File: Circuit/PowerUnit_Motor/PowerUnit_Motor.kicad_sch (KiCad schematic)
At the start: 16 parts, among them J1 Conn_01x02_Pin, J10 Conn_01x02_Pin, J11 Conn_01x02_Pin, J2 Conn_01x02_Pin, J3 Conn_01x02_Pin, J4 Conn_01x02_Pin, J5 Conn_01x02_Pin, J6 Conn_01x02_Pin, J7 Conn_01x02_Pin, J8 Conn_01x02_Pin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

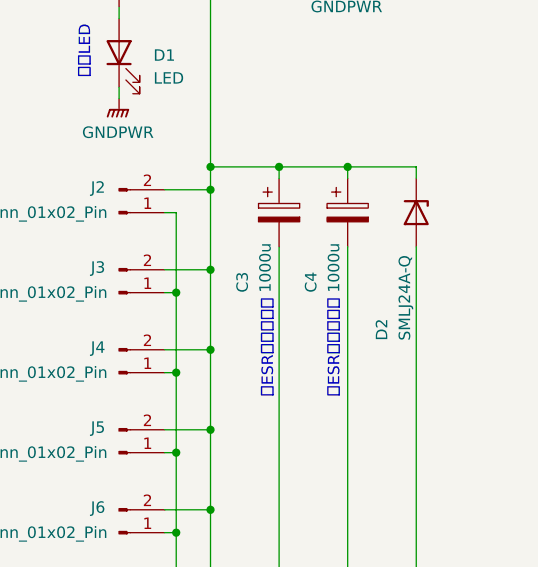
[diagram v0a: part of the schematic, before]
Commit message: Geminiに確認してもらって一部修正
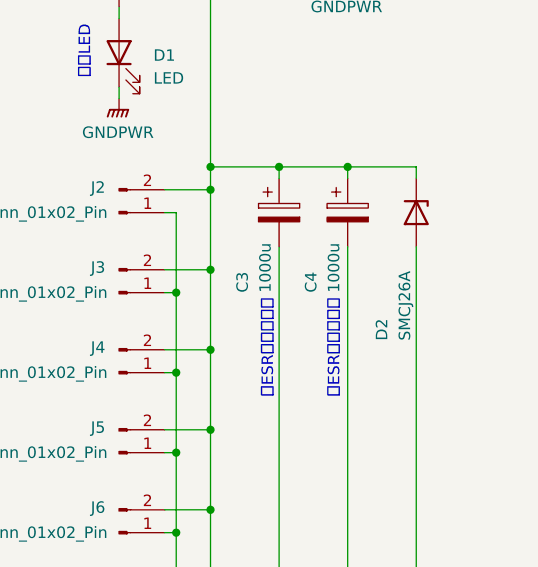
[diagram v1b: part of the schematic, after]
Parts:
- D2: value SMLJ24A-Q -> SMCJ26A; MPN_URL https://eleshop.jp/shop/g/g2839634/?srsltid=AfmBOoo6bjoT8d1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 -> https://www.digikey.jp/ja/products/detail/littelfuse-inc/SM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
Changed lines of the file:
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@@
 			)
 		)
-		(property "Value" "SMLJ24A-Q"
+		(property "Value" "SMCJ26A"
 			(at 72.39 77.724 0)
 			(show_name no)
@@
 			)
 		)
-		(property "MPN_URL" "https://eleshop.jp/shop/g/g2839634/?srsltid=AfmBOoo6bjoT8d1pyxPuT_AKB5mkWAnJWXy0-CXLNyQEAItHS72fDDjh"
+		(property "MPN_URL" "https://www.digikey.jp/ja/products/detail/littelfuse-inc/SMCJ26A/762396"
 			(at 73.66 63.5 0)
 			(hide yes)

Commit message: 発注用データを用意 発注した
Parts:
- D1: MPN_URL (none) -> https://akizukidenshi.com/catalog/g/g111333/
- J1: MPN_URL (none) -> https://akizukidenshi.com/catalog/g/g118156/
- R1: MPN_URL (none) -> https://akizukidenshi.com/catalog/g/g125752/
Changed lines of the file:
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@@
+			)
+		)
+		(property "MPN_URL" "https://akizukidenshi.com/catalog/g/g125752/"
+			(at 40.64 36.83 90)
+			(hide yes)
+			(show_name no)
+			(do_not_autoplace no)
+			(effects
+				(font
+					(size 1.27 1.27)
+				)
 			)
 		)
@@
 			)
 		)
+		(property "MPN_URL" "https://akizukidenshi.com/catalog/g/g111333/"
+			(at 40.64 45.72 90)
+			(hide yes)
+			(show_name no)
+			(do_not_autoplace no)
+			(effects
+				(font
+					(size 1.27 1.27)
+				)
+			)
+		)
 		(pin "1"
 		)
@@
 			(hide yes)
 			(show_name no)
+			(do_not_autoplace no)
+			(effects
+				(font
+					(size 1.27 1.27)
+				)
+			)
+		)
+		(property "MPN_URL" "https://akizukidenshi.com/catalog/g/g118156/"
+			(at 66.04 30.48 90)
+			(hide yes)
+			(show_name no)
